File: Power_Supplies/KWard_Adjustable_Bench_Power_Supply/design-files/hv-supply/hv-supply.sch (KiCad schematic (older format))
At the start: 12 parts, among them T1 AnTek AS-4T400 (HV), T2 AnTek AS-4T400 (Filament)

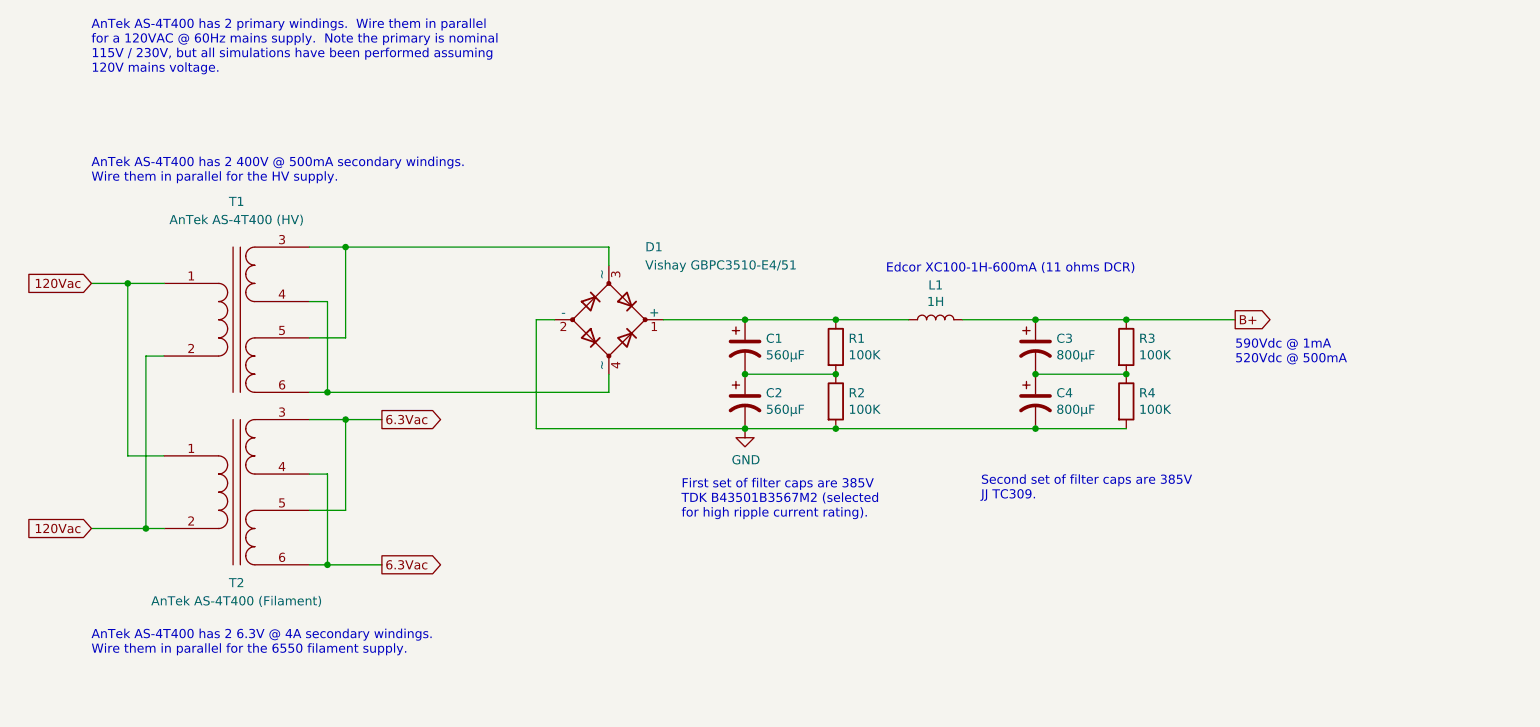
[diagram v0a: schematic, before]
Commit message: AC input for the B+ supply is "B+_120Vac".
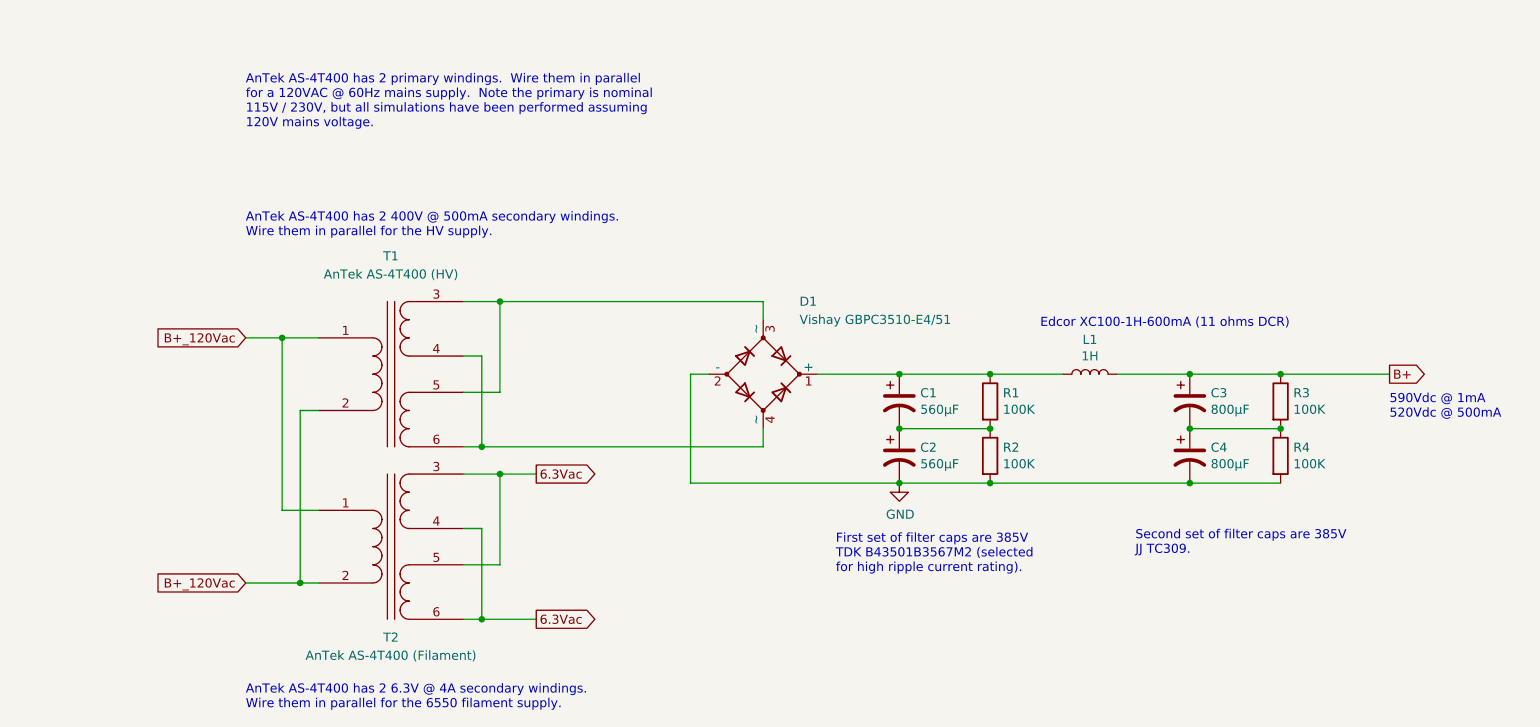
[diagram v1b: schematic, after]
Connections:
- net 120Vac renamed B+_120Vac
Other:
- moved on the sheet: C1, C2, C3, C4, D1, L1, R1, R2, R3, R4, T1, T2

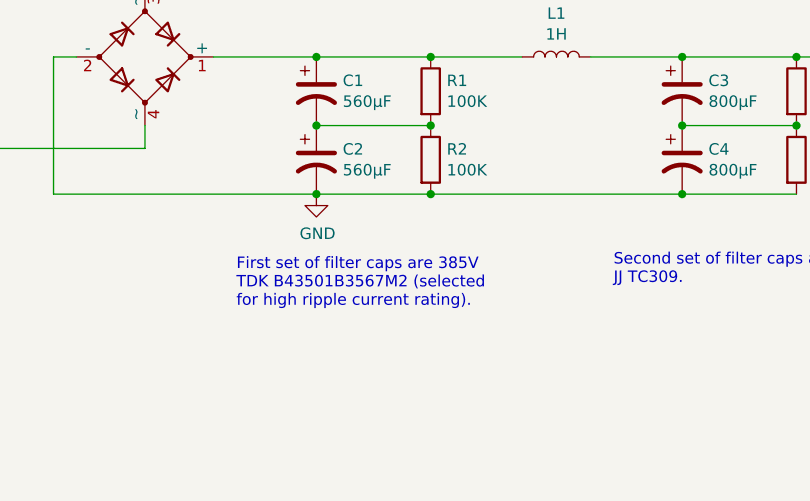
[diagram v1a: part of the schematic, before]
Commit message: Spec United Chemi-Con E92L401VSN561MR65U caps for the first filter stage; the TDK parts previously listed are EoL.
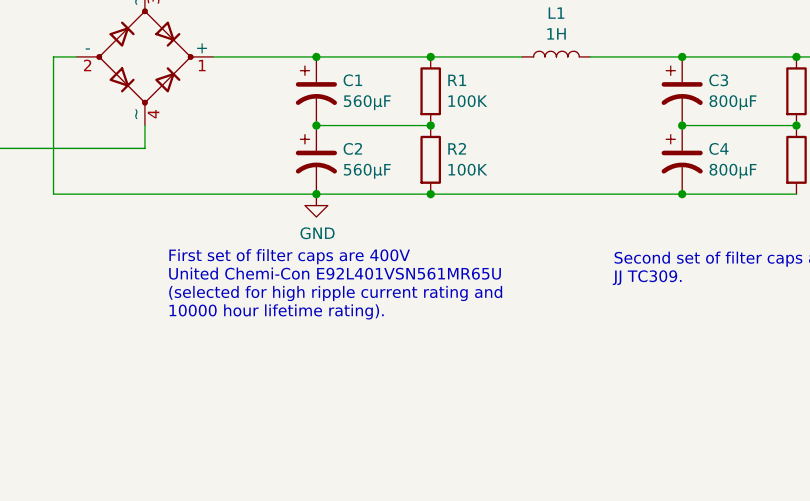
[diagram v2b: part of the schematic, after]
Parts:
- C1, C2: Mouser (none) -> 661-E92L401SN561MR65
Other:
- note added: "First set of filter caps are 400V\nUnited Chemi-Con E92L401VSN561MR65U\n(selected for high ripple current rating and\n10000 hour lifetime rating)."
- note removed: "First set of filter caps are 385V\nTDK B43501B3567M2 (selected\nfor high ripple current rating)."
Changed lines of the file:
@@
 F 2 "" H 5800 3650 50  0001 C CNN
 F 3 "~" H 5800 3650 50  0001 C CNN
+F 4 "661-E92L401SN561MR65" H 5800 3650 50  0001 C CNN "Mouser"
 	1    5800 3650
 	1    0    0    -1
@@
 F 2 "" H 5800 3950 50  0001 C CNN
 F 3 "~" H 5800 3950 50  0001 C CNN
+F 4 "661-E92L401SN561MR65" H 5800 3950 50  0001 C CNN "Mouser"
 	1    5800 3950
 	1    0    0    -1
@@
 Wire Wire Line
 	5800 4100 6300 4100
-Text Notes 5450 4600 0    50   ~ 0
-First set of filter caps are 385V\nTDK B43501B3567M2 (selected\nfor high ripple current rating).
+Text Notes 5150 4650 0    50   ~ 0
+First set of filter caps are 400V\nUnited Chemi-Con E92L401VSN561MR65U\n(selected for high ripple current rating and\n10000 hour lifetime rating).
 $Comp
 L power:GND #PWR01
